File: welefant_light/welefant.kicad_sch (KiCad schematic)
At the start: 101 parts, among them J1 Conn_01x02, J2 Conn_02x8_Odd_Even, J3 Conn_02x6_Odd_Even, Q1 AO3401A, Q2 AO3401A, Q3 AO3401A, SW1 ON-OFF, SW2 RESET, SW3 BOOT, SW4 GPIO33, SW5 GPIO33, U1 RT9080-33GJ5, U2 Audio Jack PJ-324, U3 SD18OB261-060, U4 TP4056, U5 welefant, U6 128MBit Flash, U7 ESP32-S3, U8 Reset 2.8V, X1 40 MHz

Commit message: stand
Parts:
- SW5: value GPIO33 -> IO34
- U3: footprint easyeda2kicad:MIC-SMD_SD18OB261-060 -> hacrafu:MIC-SMD_SD18OB261-060
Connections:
- net AUDIO_PWM_R: now also J2.15 (Pin_15); no longer J2.14 (Pin_14)
- net BAT_SENS: now also J2.9 (Pin_9); no longer J2.10 (Pin_10)
- net BAT_SENS_EN: now also J2.7 (Pin_7); no longer J2.9 (Pin_9)
- net GND: now also J3.4 (Pin_4); no longer J3.1 (Pin_1)
- net LED_HEAD: now also J2.4 (Pin_4); no longer J2.5 (Pin_5)
- net MIC_CLK: now also J2.10 (Pin_10); no longer J2.7 (Pin_7)
- net TX: now also J2.5 (Pin_5); no longer J2.4 (Pin_4)
- net USB_DN: now also J2.16 (Pin_16); no longer J2.15 (Pin_15)
- net USB_DP: now also J2.14 (Pin_14); no longer J2.16 (Pin_16)
- net VEXT: now also J3.1 (Pin_1); no longer J3.4 (Pin_4)
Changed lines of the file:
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@@
   (junction (at 106.68 35.56) (diameter 0) (color 0 0 0 0)
   )
+  (junction (at 273.685 147.32) (diameter 0) (color 0 0 0 0)
+  )
   (junction (at 198.12 16.51) (diameter 0) (color 0 0 0 0)
   )
@@
     (stroke (width 0) (type default))
   )
+  (wire (pts (xy 273.685 147.32) (xy 273.685 149.86))
+    (stroke (width 0) (type default))
+  )
   (wire (pts (xy 87.63 127) (xy 87.63 129.54))
     (stroke (width 0) (type default))
@@
     (stroke (width 0) (type default))
   )
-  (wire (pts (xy 253.365 147.32) (xy 260.985 147.32))
-    (stroke (width 0) (type default))
-  )
   (wire (pts (xy 208.28 35.56) (xy 208.28 41.91))
     (stroke (width 0) (type default))
@@
     (effects (font (size 1.2446 1.2446)) (justify left bottom))
   )
-  (label "USB_DP" (at 205.105 163.195 0) (fields_autoplaced)
+  (label "USB_DP" (at 205.105 160.655 0) (fields_autoplaced)
     (effects (font (size 1.27 1.27)) (justify left bottom))
   )
@@
     (effects (font (size 1.27 1.27)) (justify left bottom))
   )
-  (label "TX" (at 205.105 147.955 0) (fields_autoplaced)
-    (effects (font (size 1.27 1.27)) (justify left bottom))
+  (label "TX" (at 192.405 150.495 180) (fields_autoplaced)
+    (effects (font (size 1.27 1.27)) (justify right bottom))
   )
   (label "VEXT" (at 144.78 165.1 0) (fields_autoplaced)
@@
     (effects (font (size 1.27 1.27)) (justify right bottom))
   )
-  (label "VEXT" (at 273.685 149.86 0) (fields_autoplaced)
-    (effects (font (size 1.27 1.27)) (justify left bottom))
+  (label "VEXT" (at 260.985 147.32 180) (fields_autoplaced)
+    (effects (font (size 1.27 1.27)) (justify right bottom))
   )
   (label "V33" (at 268.605 20.955 0) (fields_autoplaced)
@@
     (effects (font (size 1.27 1.27)) (justify left bottom))
   )
-  (label "USB_DN" (at 192.405 163.195 180) (fields_autoplaced)
-    (effects (font (size 1.27 1.27)) (justify right bottom))
+  (label "USB_DN" (at 205.105 163.195 0) (fields_autoplaced)
+    (effects (font (size 1.27 1.27)) (justify left bottom))
   )
   (label "V33" (at 184.785 16.51 180) (fields_autoplaced)
@@
     (effects (font (size 1.27 1.27)) (justify left bottom))
   )
-  (label "BAT_SENS_EN" (at 192.405 155.575 180) (fields_autoplaced)
+  (label "BAT_SENS_EN" (at 192.405 153.035 180) (fields_autoplaced)
     (effects (font (size 1.27 1.27)) (justify right bottom))
   )
@@
     (effects (font (size 1.27 1.27)) (justify right bottom))
   )
-  (label "AUDIO_PWM_R" (at 205.105 160.655 0) (fields_autoplaced)
-    (effects (font (size 1.27 1.27)) (justify left bottom))
+  (label "AUDIO_PWM_R" (at 192.405 163.195 180) (fields_autoplaced)
+    (effects (font (size 1.27 1.27)) (justify right bottom))
   )
   (label "D4_LED" (at 144.78 180.34 0) (fields_autoplaced)
@@
     (effects (font (size 1.27 1.27)) (justify left bottom))
   )
-  (label "LED_HEAD" (at 192.405 150.495 180) (fields_autoplaced)
-    (effects (font (size 1.27 1.27)) (justify right bottom))
+  (label "LED_HEAD" (at 205.105 147.955 0) (fields_autoplaced)
+    (effects (font (size 1.27 1.27)) (justify left bottom))
   )
   (label "AUDIO_PWM_L" (at 192.405 160.655 180) (fields_autoplaced)
@@
     (effects (font (size 1.27 1.27)) (justify left bottom))
   )
-  (label "BAT_SENS" (at 205.105 155.575 0) (fields_autoplaced)
-    (effects (font (size 1.27 1.27)) (justify left bottom))
+  (label "BAT_SENS" (at 192.405 155.575 180) (fields_autoplaced)
+    (effects (font (size 1.27 1.27)) (justify right bottom))
   )
   (label "V33" (at 184.15 35.56 180) (fields_autoplaced)
@@
     (effects (font (size 1.2446 1.2446)) (justify right bottom))
   )
-  (label "MIC_CLK" (at 192.405 153.035 180) (fields_autoplaced)
-    (effects (font (size 1.27 1.27)) (justify right bottom))
+  (label "MIC_CLK" (at 205.105 155.575 0) (fields_autoplaced)
+    (effects (font (size 1.27 1.27)) (justify left bottom))
   )
   (label "USB_DP" (at 76.835 30.48 0) (fields_autoplaced)
@@
       (effects (font (size 1.27 1.27)))
     )
-    (property "Footprint" "easyeda2kicad:MIC-SMD_SD18OB261-060" (at 99.06 118.11 0)
+    (property "Footprint" "hacrafu:MIC-SMD_SD18OB261-060" (at 99.06 118.11 0)
       (effects (font (size 1.27 1.27)) hide)
     )
@@
     )
   )
-  (symbol (lib_id "power:GND") (at 253.365 147.32 270) (unit 1)
-    (in_bom yes) (on_board yes) (dnp no) (fields_autoplaced)
-    (property "Reference" "#PWR046" (at 247.015 147.32 0)
-      (effects (font (size 1.27 1.27)) hide)
-    )
-    (property "Value" "GND" (at 250.1901 147.32 90)
-      (effects (font (size 1.27 1.27)) (justify right))
-    )
-    (property "Footprint" "" (at 253.365 147.32 0)
-      (effects (font (size 1.27 1.27)) hide)
-    )
-    (property "Datasheet" "" (at 253.365 147.32 0)
-      (effects (font (size 1.27 1.27)) hide)
-    )
-    (pin "1")
-    (instances
-      (project "welefant"
-        (path "/97f5bd5b-f387-4518-b83a-fa60b8a606f1"
-          (reference "#PWR046") (unit 1)
-        )
-      )
-    )
-  )
   (symbol (lib_id "easyeda2kicad:CC0603KRX7R9BB104") (at 268.605 26.035 270) (mirror x) (unit 1)
     (in_bom yes) (on_board yes) (dnp no)
@@
       (effects (font (size 1.27 1.27)))
     )
-    (property "Value" "GPIO33" (at 277.495 60.96 0)
+    (property "Value" "IO34" (at 277.495 60.96 0)
       (effects (font (size 1.27 1.27)))
     )

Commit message: stand
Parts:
- added C24: 100n, easyeda2kicad:C0603, symbol easyeda2kicad:CC0603KRX7R9BB104
- added C25: 1u, easyeda2kicad:C0603, symbol easyeda2kicad:CL10A105KB8NNNC
- J2: value Conn_02x8_Odd_Even -> Conn_02x7_Odd_Even; footprint hacrafu:PinHeader_2x08_P2.54mm_Vertical_SMD_handsolder -> hacrafu:PinHeader_2x07_P2.54mm_Vertical_SMD_handsolder; symbol Connector_Generic:Conn_02x08_Odd_Even -> Connector_Generic:Conn_02x07_Odd_Even
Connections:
- net AUDIO_PWM_L: now also J2.12 (Pin_12); no longer J2.13 (Pin_13)
- net AUDIO_PWM_R: now also J2.11 (Pin_11); no longer J2.15 (Pin_15)
- net BAT_SENS: now also J2.6 (Pin_6); no longer J2.9 (Pin_9)
- net GND: now also C24.2, C25.2
- net JACK_SENS: now also J2.9 (Pin_9); no longer J2.11 (Pin_11)
- net LED: no longer J2.12 (Pin_12)
- net LED_HEAD: no longer J2.4 (Pin_4)
- net LED_MATRIX: no longer J2.6 (Pin_6)
- net USB_DN: now also J2.14 (Pin_14); no longer J2.16 (Pin_16)
- net USB_DP: now also J2.13 (Pin_13); no longer J2.14 (Pin_14)
- net V5: now also J2.4 (Pin_4)
- net VEXT: now also C24.1, C25.1
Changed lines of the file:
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@@
     (stroke (width 0) (type default))
   )
+  (wire (pts (xy 49.53 182.88) (xy 53.975 182.88))
+    (stroke (width 0) (type default))
+  )
+  (wire (pts (xy 109.22 106.68) (xy 115.57 106.68))
+    (stroke (width 0) (type default))
+  )
   (wire (pts (xy 55.88 190.5) (xy 55.88 193.04))
     (stroke (width 0) (type default))
@@
     (stroke (width 0) (type default))
   )
+  (wire (pts (xy 115.57 96.52) (xy 118.745 96.52))
+    (stroke (width 0) (type default))
+  )
   (wire (pts (xy 20.32 55.88) (xy 21.59 55.88))
     (stroke (width 0) (type default))
@@
     (effects (font (size 1.27 1.27)) (justify right bottom))
   )
-  (label "LED" (at 205.105 158.115 0) (fields_autoplaced)
-    (effects (font (size 1.27 1.27)) (justify left bottom))
-  )
   (label "BAT_SENS" (at 220.98 69.85 180) (fields_autoplaced)
     (effects (font (size 1.27 1.27)) (justify right bottom))
@@
     (effects (font (size 1.2446 1.2446)) (justify left bottom))
   )
-  (label "USB_DP" (at 205.105 160.655 0) (fields_autoplaced)
-    (effects (font (size 1.27 1.27)) (justify left bottom))
+  (label "USB_DP" (at 192.405 160.655 180) (fields_autoplaced)
+    (effects (font (size 1.27 1.27)) (justify right bottom))
   )
   (label "VEXT" (at 49.53 177.8 0) (fields_autoplaced)
@@
     (effects (font (size 1.27 1.27)) (justify left bottom))
   )
+  (label "VEXT" (at 81.28 139.7 0) (fields_autoplaced)
+    (effects (font (size 1.27 1.27)) (justify left bottom))
+  )
   (label "BAT_SENS_EN" (at 123.19 82.55 270) (fields_autoplaced)
     (effects (font (size 1.27 1.27)) (justify right bottom))
@@
     (effects (font (size 1.27 1.27)) (justify left bottom))
   )
-  (label "USB_DN" (at 205.105 163.195 0) (fields_autoplaced)
+  (label "USB_DN" (at 205.105 160.655 0) (fields_autoplaced)
+    (effects (font (size 1.27 1.27)) (justify left bottom))
+  )
+  (label "V5" (at 205.105 147.955 0) (fields_autoplaced)
     (effects (font (size 1.27 1.27)) (justify left bottom))
   )
@@
     (effects (font (size 1.27 1.27)) (justify right bottom))
   )
-  (label "AUDIO_PWM_R" (at 192.405 163.195 180) (fields_autoplaced)
+  (label "AUDIO_PWM_R" (at 192.405 158.115 180) (fields_autoplaced)
     (effects (font (size 1.27 1.27)) (justify right bottom))
   )
@@
     (effects (font (size 1.27 1.27)) (justify left bottom))
   )
-  (label "LED_HEAD" (at 205.105 147.955 0) (fields_autoplaced)
-    (effects (font (size 1.27 1.27)) (justify left bottom))
-  )
-  (label "AUDIO_PWM_L" (at 192.405 160.655 180) (fields_autoplaced)
-    (effects (font (size 1.27 1.27)) (justify right bottom))
-  )
-  (label "VEXT" (at 81.28 139.7 0) (fields_autoplaced)
+  (label "AUDIO_PWM_L" (at 205.105 158.115 0) (fields_autoplaced)
     (effects (font (size 1.27 1.27)) (justify left bottom))
   )
@@
     (effects (font (size 1.27 1.27)) (justify left bottom))
   )
-  (label "LED_MATRIX" (at 205.105 150.495 0) (fields_autoplaced)
-    (effects (font (size 1.27 1.27)) (justify left bottom))
-  )
   (label "VBAT" (at 129.54 62.865 0) (fields_autoplaced)
     (effects (font (size 1.27 1.27)) (justify left bottom))
@@
     (effects (font (size 1.27 1.27)) (justify left bottom))
   )
-  (label "JACK_SENS" (at 192.405 158.115 180) (fields_autoplaced)
+  (label "JACK_SENS" (at 192.405 155.575 180) (fields_autoplaced)
     (effects (font (size 1.27 1.27)) (justify right bottom))
   )
@@
     (effects (font (size 1.27 1.27)) (justify left bottom))
   )
-  (label "BAT_SENS" (at 192.405 155.575 180) (fields_autoplaced)
-    (effects (font (size 1.27 1.27)) (justify right bottom))
+  (label "BAT_SENS" (at 205.105 150.495 0) (fields_autoplaced)
+    (effects (font (size 1.27 1.27)) (justify left bottom))
   )
   (label "V33" (at 184.15 35.56 180) (fields_autoplaced)
@@
     )
   )
+  (symbol (lib_id "easyeda2kicad:CC0603KRX7R9BB104") (at 115.57 101.6 270) (mirror x) (unit 1)
+    (in_bom yes) (on_board yes) (dnp no)
+    (property "Reference" "C24" (at 110.49 99.695 90)
+      (effects (font (size 1.27 1.27)) (justify left))
+    )
+    (property "Value" "100n" (at 109.22 102.87 90)
+      (effects (font (size 1.27 1.27)) (justify left))
+    )
+    (property "Footprint" "easyeda2kicad:C0603" (at 107.95 101.6 0)
+      (effects (font (size 1.27 1.27)) hide)
+    )
+    (property "Datasheet" "https://lcsc.com/product-detail/Multilayer-Ceramic-Capacitors-MLCC-SMD-SMT_100nF-104-10-50V_C14663.html" (at 105.41 101.6 0)
+      (effects (font (size 1.27 1.27)) hide)
+    )
+    (property "Manufacturer" "YAGEO(国巨)" (at 102.87 101.6 0)
+      (effects (font (size 1.27 1.27)) hide)
+    )
+    (property "LCSC Part" "C14663" (at 100.33 101.6 0)
+      (effects (font (size 1.27 1.27)) hide)
+    )
+    (property "JLC Part" "Basic Part" (at 97.79 101.6 0)
+      (effects (font (size 1.27 1.27)) hide)
+    )
+    (pin "1")
+    (pin "2")
+    (instances
+      (project "welefant"
+        (path "/97f5bd5b-f387-4518-b83a-fa60b8a606f1"
+          (reference "C24") (unit 1)
+        )
+      )
+    )
+  )
   (symbol (lib_id "easyeda2kicad:TS-1187A-B-A-B") (at 193.04 73.66 0) (unit 1)
     (in_bom yes) (on_board yes) (dnp no)
@@
     )
   )
-  (symbol (lib_id "Connector_Generic:Conn_02x08_Odd_Even") (at 197.485 153.035 0) (unit 1)
+  (symbol (lib_id "Connector_Generic:Conn_02x07_Odd_Even") (at 197.485 153.035 0) (unit 1)
     (in_bom yes) (on_board yes) (dnp no)
     (property "Reference" "J2" (at 198.755 139.7 0)
       (effects (font (size 1.27 1.27)))
     )
-    (property "Value" "Conn_02x8_Odd_Even" (at 198.755 141.605 0)
+    (property "Value" "Conn_02x7_Odd_Even" (at 198.755 141.605 0)
       (effects (font (size 1.27 1.27)))
     )
-    (property "Footprint" "hacrafu:PinHeader_2x08_P2.54mm_Vertical_SMD_handsolder" (at 197.485 153.035 0)
+    (property "Footprint" "hacrafu:PinHeader_2x07_P2.54mm_Vertical_SMD_handsolder" (at 197.485 153.035 0)
       (effects (font (size 1.27 1.27)) hide)
     )
@@
     (pin "13")
     (pin "14")
-    (pin "15")
-    (pin "16")
     (pin "2")
     (pin "3")
@@
     )
   )
+  (symbol (lib_id "power:GND") (at 53.975 182.88 0) (unit 1)
+    (in_bom yes) (on_board yes) (dnp no) (fields_autoplaced)
+    (property "Reference" "#PWR067" (at 53.975 189.23 0)
+      (effects (font (size 1.27 1.27)) hide)
+    )
+    (property "Value" "GND" (at 53.975 187.0131 0)
+      (effects (font (size 1.27 1.27)))
+    )
+    (property "Footprint" "" (at 53.975 182.88 0)
+      (effects (font (size 1.27 1.27)) hide)
+    )
+    (property "Datasheet" "" (at 53.975 182.88 0)
+      (effects (font (size 1.27 1.27)) hide)
+    )
+    (pin "1")
+    (instances
+      (project "welefant"
+        (path "/97f5bd5b-f387-4518-b83a-fa60b8a606f1"
+          (reference "#PWR067") (unit 1)
+        )
+      )
+    )
+  )
   (symbol (lib_id "power:GND") (at 88.9 107.95 270) (unit 1)
     (in_bom yes) (on_board yes) (dnp no)
@@
     )
   )
+  (symbol (lib_id "easyeda2kicad:CL10A105KB8NNNC") (at 49.53 186.69 270) (mirror x) (unit 1)
+    (in_bom yes) (on_board yes) (dnp no)
+    (property "Reference" "C25" (at 53.34 185.42 90)
+      (effects (font (size 1.27 1.27)) (justify right))
+    )
+    (property "Value" "1u" (at 49.53 185.42 90)
+      (effects (font (size 1.27 1.27)) (justify right))
+    )
+    (property "Footprint" "easyeda2kicad:C0603" (at 41.91 186.69 0)
+      (effects (font (size 1.27 1.27)) hide)
+    )
+    (property "Datasheet" "https://lcsc.com/product-detail/Multilayer-Ceramic-Capacitors-MLCC-SMD-SMT_SAMSUNG_CL10A105KB8NNNC_1uF-105-10-50V_C15849.html" (at 39.37 186.69 0)
+      (effects (font (size 1.27 1.27)) hide)
+    )
+    (property "Manufacturer" "SAMSUNG(三星)" (at 36.83 186.69 0)
+      (effects (font (size 1.27 1.27)) hide)
+    )
+    (property "LCSC Part" "C15849" (at 34.29 186.69 0)
+      (effects (font (size 1.27 1.27)) hide)
+    )
+    (property "JLC Part" "Basic Part" (at 31.75 186.69 0)
+      (effects (font (size 1.27 1.27)) hide)
+    )
+    (pin "1")
+    (pin "2")
+    (instances
+      (project "welefant"
+        (path "/97f5bd5b-f387-4518-b83a-fa60b8a606f1"
+          (reference "C25") (unit 1)
+        )
+      )
+    )
+  )
   (symbol (lib_id "hacrafu:SK6812MINI-E") (at 39.37 167.64 0) (mirror y) (unit 1)
     (in_bom yes) (on_board yes) (dnp no) (fields_autoplaced)
@@
     )
     (pin "0")
-    (pin "13")
+    (pin "1")
     (pin "2")
     (pin "3")
@@
         )
       )
+    )
+  )
+  (symbol (lib_id "power:GND") (at 118.745 96.52 0) (unit 1)
+    (in_bom yes) (on_board yes) (dnp no)
+    (property "Reference" "#PWR046" (at 118.745 102.87 0)
+      (effects (font (size 1.27 1.27)) hide)
+    )
+    (property "Value" "GND" (at 118.745 99.695 90)
+      (effects (font (size 1.27 1.27)) (justify right))
+    )
+    (property "Footprint" "" (at 118.745 96.52 0)
+      (effects (font (size 1.27 1.27)) hide)
+    )
+    (property "Datasheet" "" (at 118.745 96.52 0)
+      (effects (font (size 1.27 1.27)) hide)
+    )
+    (pin "1")
+    (instances
+      (project "welefant"
+        (path "/97f5bd5b-f387-4518-b83a-fa60b8a606f1"
+          (reference "#PWR046") (unit 1)
+        )
+      )

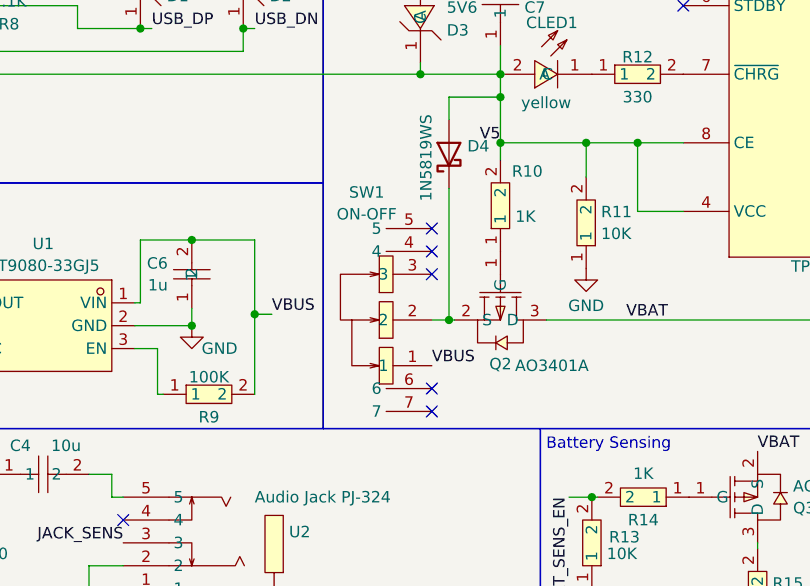
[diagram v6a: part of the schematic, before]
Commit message: muss jetzt auf ESP32-S3FH4R2 umstellen
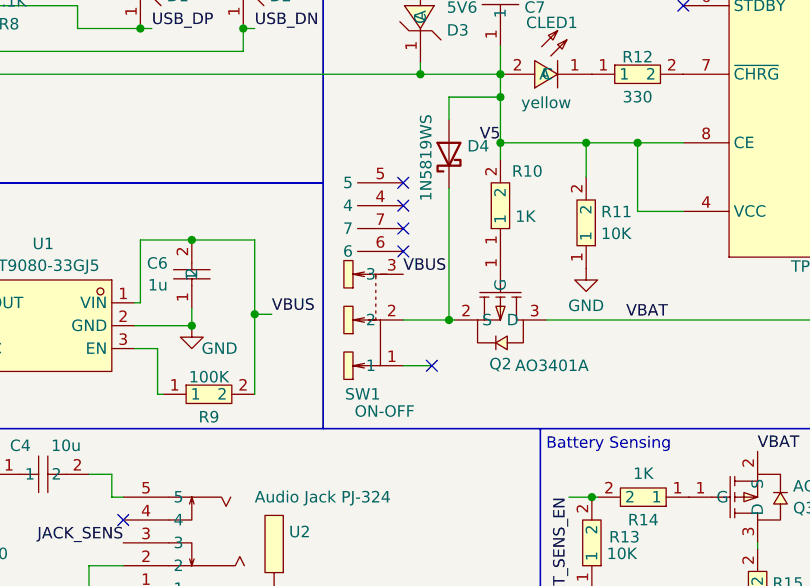
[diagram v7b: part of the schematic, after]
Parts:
- removed SW1: ON-OFF, easyeda2kicad:SW-SMD_MK-12C02-G025, symbol easyeda2kicad:MK-12C02-G025
- added SW1: ON-OFF, easyeda2kicad:SW-TH_K3-1296S-E1, symbol easyeda2kicad:K3-1296S-E1_C128955
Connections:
- net VBUS: now also SW1.3
- net at D4.1 (K), Q2.2 (S): now also SW1.2
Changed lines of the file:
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@@
   (no_connect (at 54.61 66.04))
   (no_connect (at 27.94 25.4))
-  (no_connect (at 107.95 70.485))
+  (no_connect (at 104.775 47.625))
   (no_connect (at 38.1 13.97))
-  (no_connect (at 107.95 52.705))
-  (no_connect (at 107.95 55.245))
-  (no_connect (at 107.95 57.785))
+  (no_connect (at 104.775 52.705))
+  (no_connect (at 104.775 55.245))
+  (no_connect (at 104.775 50.165))
   (no_connect (at 220.98 102.87))
   (no_connect (at 113.03 129.54))
@@
   (no_connect (at 40.64 44.45))
   (no_connect (at 220.98 52.07))
-  (no_connect (at 107.95 73.025))
+  (no_connect (at 107.95 67.945))
   (no_connect (at 135.89 27.94))
   (no_connect (at 144.78 193.04))
@@
     (stroke (width 0) (type default))
   )
+  (wire (pts (xy 104.775 67.945) (xy 107.95 67.945))
+    (stroke (width 0) (type default))
+  )
   (wire (pts (xy 165.735 112.395) (xy 167.64 112.395))
     (stroke (width 0) (type default))
@@
     (stroke (width 0) (type default))
   )
-  (wire (pts (xy 107.95 62.865) (xy 109.855 62.865))
+  (wire (pts (xy 104.775 62.865) (xy 109.855 62.865))
     (stroke (width 0) (type default))
   )
@@
     (effects (font (size 1.27 1.27)) (justify left bottom))
   )
-  (label "VBUS" (at 107.95 67.945 0) (fields_autoplaced)
+  (label "VBUS" (at 104.775 57.785 0) (fields_autoplaced)
     (effects (font (size 1.27 1.27)) (justify left bottom))
   )
@@
     )
     (pin "0")
-    (pin "1")
     (pin "2")
     (pin "3")
@@
     (pin "B8")
     (pin "B9")
+    (pin "1")
     (instances
       (project "welefant"
@@
     )
   )
+  (symbol (lib_id "easyeda2kicad:K3-1296S-E1_C128955") (at 102.235 57.785 270) (mirror x) (unit 1)
+    (in_bom yes) (on_board yes) (dnp no)
+    (property "Reference" "SW1" (at 102.235 71.12 90)
+      (effects (font (size 1.27 1.27)) (justify right))
+    )
+    (property "Value" "ON-OFF" (at 106.045 73.025 90)
+      (effects (font (size 1.27 1.27)) (justify right))
+    )
+    (property "Footprint" "easyeda2kicad:SW-TH_K3-1296S-E1" (at 97.155 57.785 0)
+      (effects (font (size 1.27 1.27)) hide)
+    )
+    (property "Datasheet" "https://lcsc.com/product-detail/Toggle-Switches_Korean-Hroparts-Elec-K3-1296S-E1_C128955.html" (at 94.615 57.785 0)
+      (effects (font (size 1.27 1.27)) hide)
+    )
+    (property "LCSC Part" "C128955" (at 92.075 57.785 0)
+      (effects (font (size 1.27 1.27)) hide)
+    )
+    (pin "1")
+    (pin "2")
+    (pin "3")
+    (pin "4")
+    (pin "5")
+    (pin "6")
+    (pin "7")
+    (instances
+      (project "welefant"
+        (path "/97f5bd5b-f387-4518-b83a-fa60b8a606f1"
+          (reference "SW1") (unit 1)
+        )
+      )
+    )
+  )
   (symbol (lib_id "power:GND") (at 29.21 180.34 0) (unit 1)
     (in_bom yes) (on_board yes) (dnp no) (fields_autoplaced)
@@
         )
       )
-    )
-  )
-  (symbol (lib_id "easyeda2kicad:MK-12C02-G025") (at 102.87 62.865 90) (unit 1)
-    (in_bom yes) (on_board yes) (dnp no) (fields_autoplaced)
-    (property "Reference" "SW1" (at 100.711 48.6877 90)
-      (effects (font (size 1.27 1.27)))
-    )
-    (property "Value" "ON-OFF" (at 100.711 51.1119 90)
-      (effects (font (size 1.27 1.27)))
-    )
-    (property "Footprint" "easyeda2kicad:SW-SMD_MK-12C02-G025" (at 115.57 62.865 0)
-      (effects (font (size 1.27 1.27)) hide)
-    )
-    (property "Datasheet" "https://lcsc.com/product-detail/Toggle-Switches_G-Switch-MK-12C02-G025_C778186.html" (at 118.11 62.865 0)
-      (effects (font (size 1.27 1.27)) hide)
-    )
-    (property "LCSC Part" "C778186" (at 120.65 62.865 0)
-      (effects (font (size 1.27 1.27)) hide)
-    )
-    (pin "1")
-    (pin "2")
-    (pin "3")
-    (pin "4")
-    (pin "5")
-    (pin "6")
-    (pin "7")
-    (instances
-      (project "welefant"
-        (path "/97f5bd5b-f387-4518-b83a-fa60b8a606f1"
-          (reference "SW1") (unit 1)
-        )
-      )
